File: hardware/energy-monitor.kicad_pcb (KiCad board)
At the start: 2 copper layers, 40 x 40 mm, 36 parts, among them P1 CON-SENSOR2, P3 BOOT, P4 DEBUG, U1 XMC110024, U2 TLV272IS, U3 DRILL, U4 DRILL, U5 DRILL, U6 DRILL, U7 phone-jack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

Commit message: fix sym lib table, change pcb texts
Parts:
- moved G*** 33.5 mm to (146.4, 73.9)
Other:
- board text added: "AC Current max 1V"
- board text added: "AC Voltage max 12VAC"
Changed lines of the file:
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@@
   (general
     (thickness 1.6)
-    (drawings 11)
+    (drawings 13)
     (tracks 228)
     (zones 0)
@@
   )
   (layers
-    (0 F.Cu signal)
-    (31 B.Cu signal)
+    (0 F.Cu signal hide)
+    (31 B.Cu signal hide)
     (32 B.Adhes user)
     (33 F.Adhes user)
@@
   )
   (setup
-    (last_trace_width 0.2)
+    (last_trace_width 0.25)
     (user_trace_width 0.2)
     (user_trace_width 0.3)
@@
   )
   (module kicad-libraries:Logo_31x31 (layer F.Cu)
-    (at 165.8 101.2)
+    (at 146.4 73.9)
     (fp_text reference G*** (at 0 0) (layer F.SilkS) hide
       (effects (font (size 1.524 1.524) (thickness 0.3)))
@@
       (xy -0.55372 -1.41224) (xy -0.55372 -1.67132)) (layer B.SilkS) (width 0.00254))
   )
-  (gr_text "Energy Monitor 1.0" (at 165.8 66.4) (layer F.SilkS)
+  (gr_text "AC Current\nmax 1V\n" (at 167.4 71.8) (layer F.SilkS)
     (effects (font (size 0.8 0.8) (thickness 0.15)))
   )
-  (gr_text tinkerforge.com (at 165.8 103.6) (layer F.SilkS)
+  (gr_text "AC Voltage max 12VAC" (at 172.3 88.6) (layer F.SilkS)
     (effects (font (size 0.8 0.8) (thickness 0.15)))
   )
+  (gr_text "Energy Monitor 1.0" (at 146.6 93) (layer F.SilkS)
+    (effects (font (size 0.8 0.8) (thickness 0.15)))
+  )
+  (gr_text tinkerforge.com (at 146.4 76.6) (layer F.SilkS)
+    (effects (font (size 0.8 0.8) (thickness 0.15)))
+  )

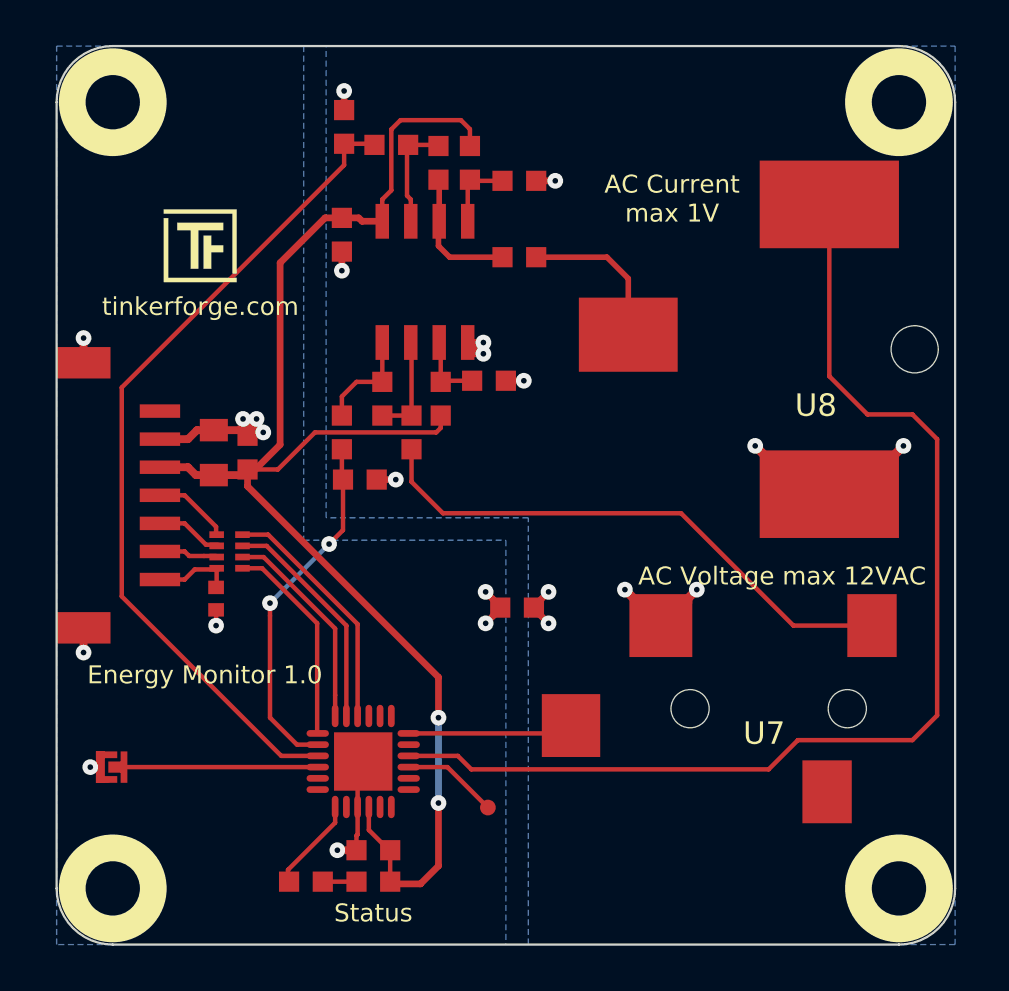
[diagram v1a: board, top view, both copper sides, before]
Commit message: changed text layout, added fiducialmarks, ready for prototype
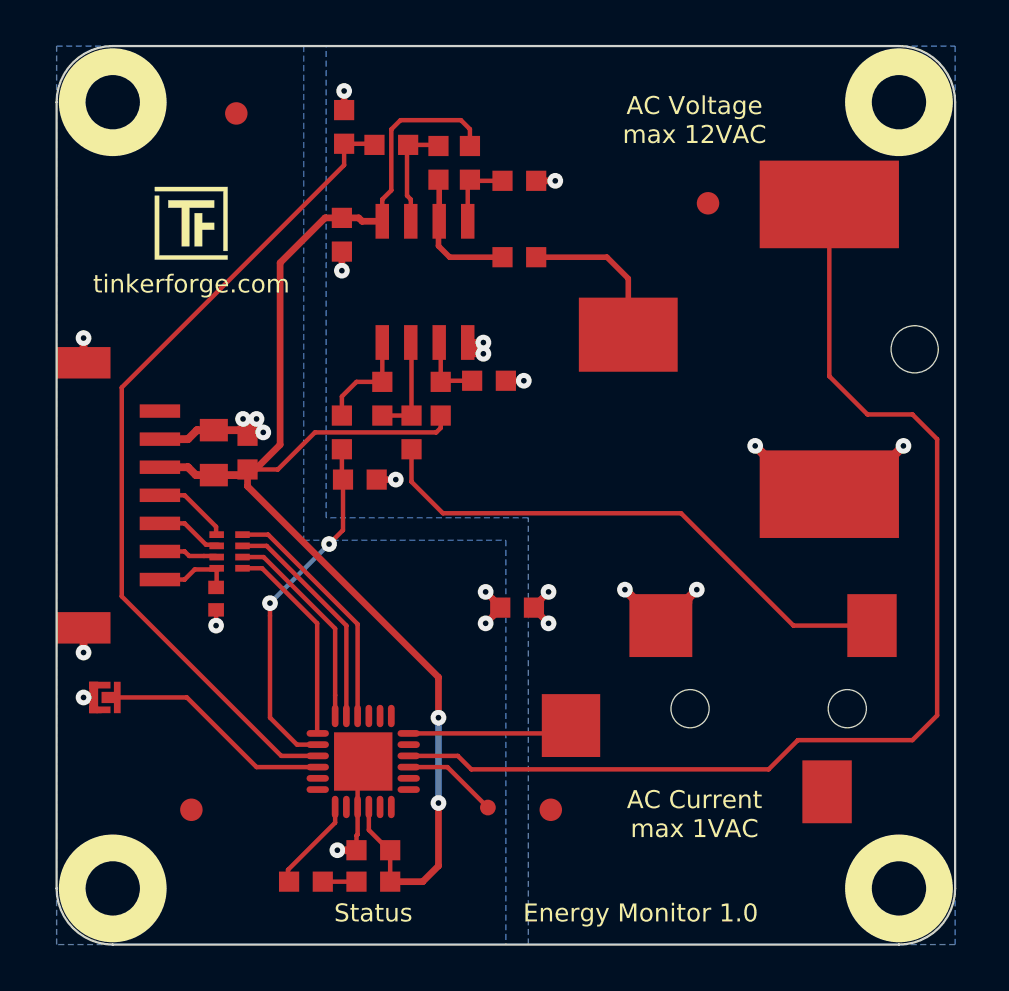
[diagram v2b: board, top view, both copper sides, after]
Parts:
- added Fiducial_Mark: VAL**, kicad-libraries:Fiducial_Mark, F.Cu at (148.0, 68.0)
- added Fiducial_Mark: VAL**, kicad-libraries:Fiducial_Mark, F.Cu at (146.0, 99.0)
- added Fiducial_Mark: VAL**, kicad-libraries:Fiducial_Mark, F.Cu at (169.0, 72.0)
- added Fiducial_Mark: VAL**, kicad-libraries:Fiducial_Mark, F.Cu at (162.0, 99.0)
- moved P3 3.11 mm to (142.2, 94.0)
- moved G*** 1.08 mm to (146.0, 72.9)
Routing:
- net Net-(P3-Pad2): track 8.93 -> 10.6 mm
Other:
- board text added: "AC Current max 1VAC"
- board text removed: "AC Current max 1V"

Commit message: changed resistor value for voltage measurement
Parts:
- R10, R9: value 3,9k -> 9,1k
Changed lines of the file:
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@@
   )
   (layers
-    (0 F.Cu signal)
+    (0 F.Cu signal hide)
     (31 B.Cu signal)
     (32 B.Adhes user)
-    (33 F.Adhes user)
+    (33 F.Adhes user hide)
     (34 B.Paste user)
-    (35 F.Paste user)
+    (35 F.Paste user hide)
     (36 B.SilkS user)
-    (37 F.SilkS user)
+    (37 F.SilkS user hide)
     (38 B.Mask user)
-    (39 F.Mask user)
+    (39 F.Mask user hide)
     (40 Dwgs.User user)
     (41 Cmts.User user)
@@
       (effects (font (size 0.2 0.2) (thickness 0.05)))
     )
-    (fp_text value 3,9k (at 0.05 -0.375 90) (layer F.Fab)
+    (fp_text value 9,1k (at 0.05 -0.375 90) (layer F.Fab)
       (effects (font (size 0.2 0.2) (thickness 0.05)))
     )
@@
       (effects (font (size 0.2 0.2) (thickness 0.05)))
     )
-    (fp_text value 3,9k (at 0.05 -0.375) (layer F.Fab)
-      (effects (font (size 0.2 0.2) (thickness 0.05)))
-    )
+    (fp_text value 9,1k (at 0.05 -0.375) (layer F.Fab)
+      (effects (font (size 0.2 0.2) (thickness 0.05)))
+    )

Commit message: changed resistor values
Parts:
- R3: value 22k -> 91k
- R4: value 3k -> 9,1k
- R5: value 15k -> 68k
- R6: value 12k -> 33k
- R9: value 9,1k -> 5,6k
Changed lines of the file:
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@@
       (effects (font (size 0.2 0.2) (thickness 0.05)))
     )
-    (fp_text value 22k (at 0.05 -0.375 270) (layer F.Fab)
+    (fp_text value 91k (at 0.05 -0.375 270) (layer F.Fab)
       (effects (font (size 0.2 0.2) (thickness 0.05)))
     )
@@
       (effects (font (size 0.2 0.2) (thickness 0.05)))
     )
-    (fp_text value 3k (at 0.05 -0.375) (layer F.Fab)
+    (fp_text value 9,1k (at 0.05 -0.375) (layer F.Fab)
       (effects (font (size 0.2 0.2) (thickness 0.05)))
     )
@@
       (effects (font (size 0.2 0.2) (thickness 0.05)))
     )
-    (fp_text value 15k (at 0.05 -0.375 270) (layer F.Fab)
+    (fp_text value 68k (at 0.05 -0.375 270) (layer F.Fab)
       (effects (font (size 0.2 0.2) (thickness 0.05)))
     )
@@
       (effects (font (size 0.2 0.2) (thickness 0.05)))
     )
-    (fp_text value 12k (at 0.05 -0.375 270) (layer F.Fab)
+    (fp_text value 33k (at 0.05 -0.375 270) (layer F.Fab)
       (effects (font (size 0.2 0.2) (thickness 0.05)))
     )
@@
       (effects (font (size 0.2 0.2) (thickness 0.05)))
     )
-    (fp_text value 9,1k (at 0.05 -0.375 90) (layer F.Fab)
+    (fp_text value 5,6k (at 0.05 -0.375 90) (layer F.Fab)
       (effects (font (size 0.2 0.2) (thickness 0.05)))
     )

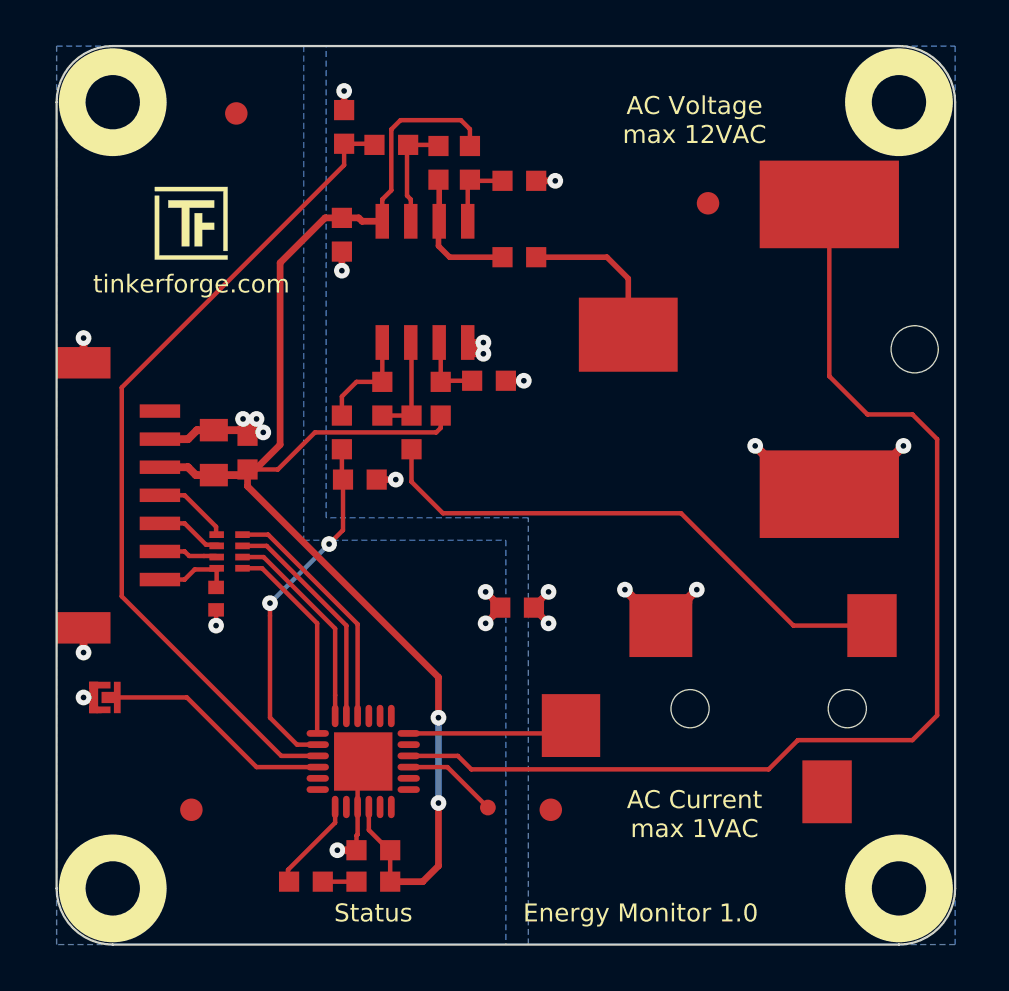
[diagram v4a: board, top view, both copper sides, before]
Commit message: changed resistor values, bigger footprint for dc-033, changed labeling
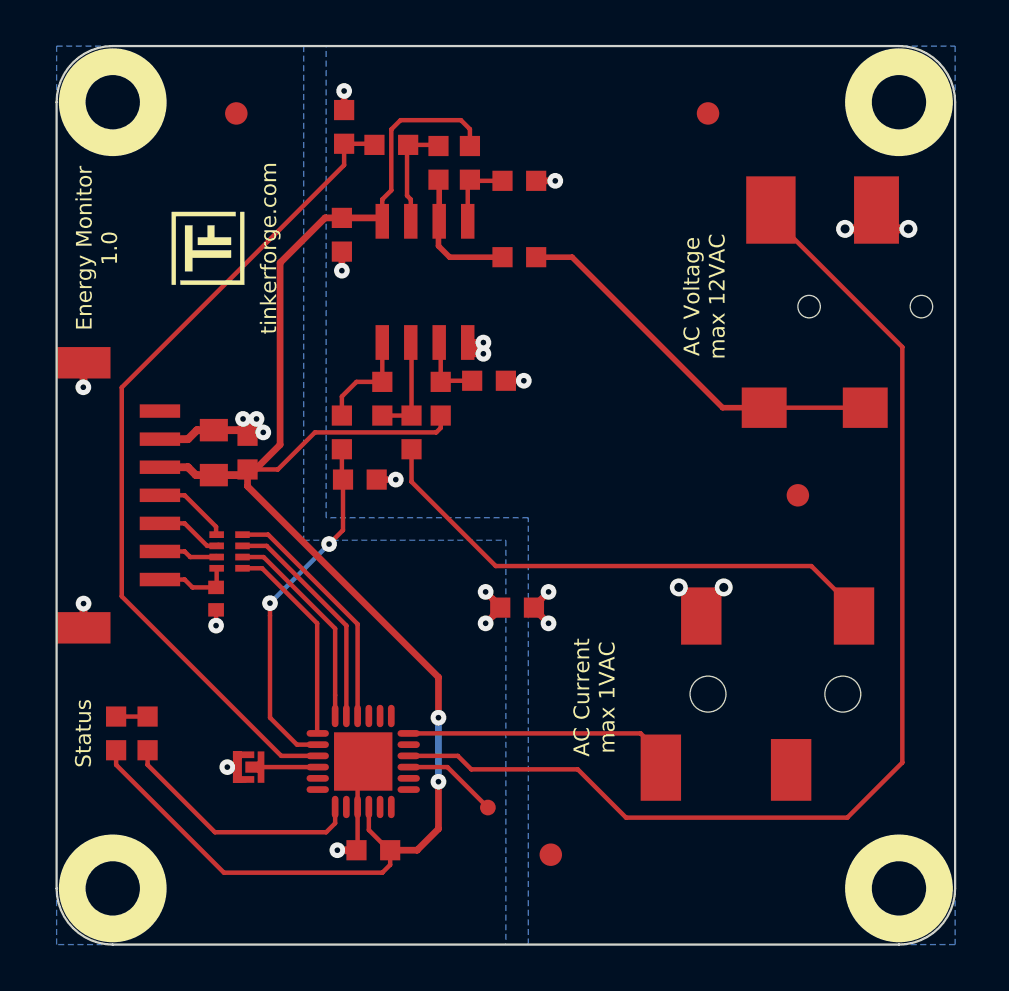
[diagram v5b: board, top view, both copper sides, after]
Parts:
- U7: footprint kicad-libraries:SJ-3524-SMT -> kicad-libraries:PJ-327C-3
- U8: footprint kicad-libraries:PJ-036AH-SMT -> kicad-libraries:DC-033
- moved Fiducial_Mark 30.4 mm to (173.0, 85.0)
- moved D3 13.2 mm to (142.7, 95.6), turned to 90 degrees
- moved G*** 9.91 mm to (160.0, 78.0), turned to 270 degrees
- moved R8 9.66 mm to (144.1, 95.6), turned to 90 degrees
- moved VAL 9.04 mm to (160.0, 91.4), turned to 270 degrees
- moved P3 7.11 mm to (148.6, 97.1)
- moved U8 6.51 mm to (180.0, 76.6)
- moved Fiducial_Mark 4.00 mm to (169.0, 68.0)
- moved U7 3.84 mm to (177.5, 93.8)
- moved Fiducial_Mark 2.00 mm to (162.0, 101.0)
- moved G*** 1.33 mm to (146.8, 74.0), turned to 90 degrees
- turned VAL to 270 degrees
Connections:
- P1 pad 1: (no net) -> +5V
- U1 pad 11: (no net) -> Net-(U1-Pad11)
- U1 pad 12: (no net) -> Net-(U1-Pad12)
- U1 pad 13: (no net) -> Net-(U1-Pad13)
- U1 pad 14: (no net) -> Net-(U1-Pad14)
- U1 pad 17: (no net) -> Net-(U1-Pad17)
- U1 pad 19: (no net) -> Net-(U1-Pad19)
- U1 pad 20: (no net) -> Net-(U1-Pad20)
- U1 pad 21: (no net) -> Net-(U1-Pad21)
- U1 pad 5: (no net) -> Net-(U1-Pad5)
- U1 pad 6: (no net) -> Net-(U1-Pad6)
- U1 pad 8: (no net) -> Net-(U1-Pad8)
- U7 pad 3: (no net) -> AGND
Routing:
- net 3V3: track 65.7 -> 78.3 mm
- net Net-(R11-Pad1): track 6.94 -> 18.1 mm
- net Net-(P3-Pad2): track 10.6 -> 3.22 mm
- net Net-(R8-Pad1): track 4.19 -> 11.1 mm
- net AGND: track 21.6 -> 16.5 mm
- net PlugA: track 7.55 -> 12.4 mm
- net PlugV: track 50.4 -> 51.2 mm
- net Net-(R5-Pad2): track 24.6 -> 23.9 mm
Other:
- net class Default: clearance 0.2 -> 0.149
- rule trace_clearance: 0.2 -> 0.149

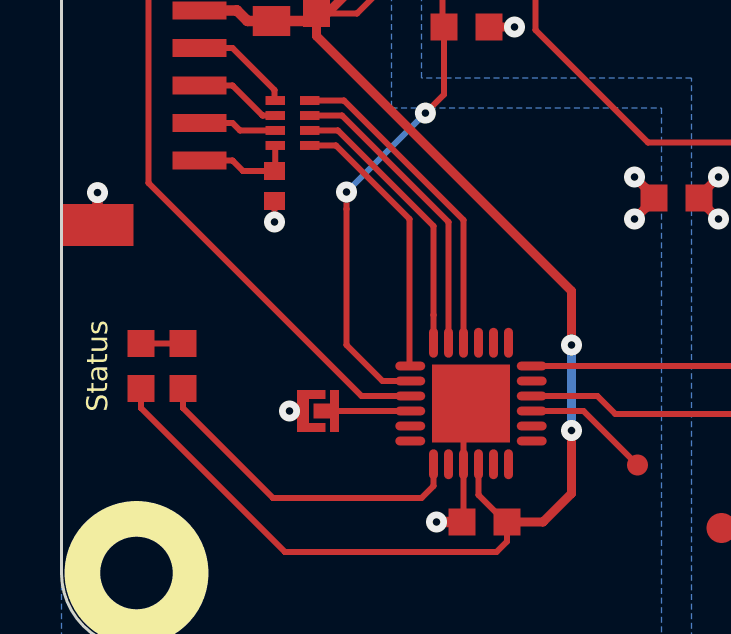
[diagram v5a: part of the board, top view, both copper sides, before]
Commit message: changed AnalogV pin from 2.2 to 2.7/2.8
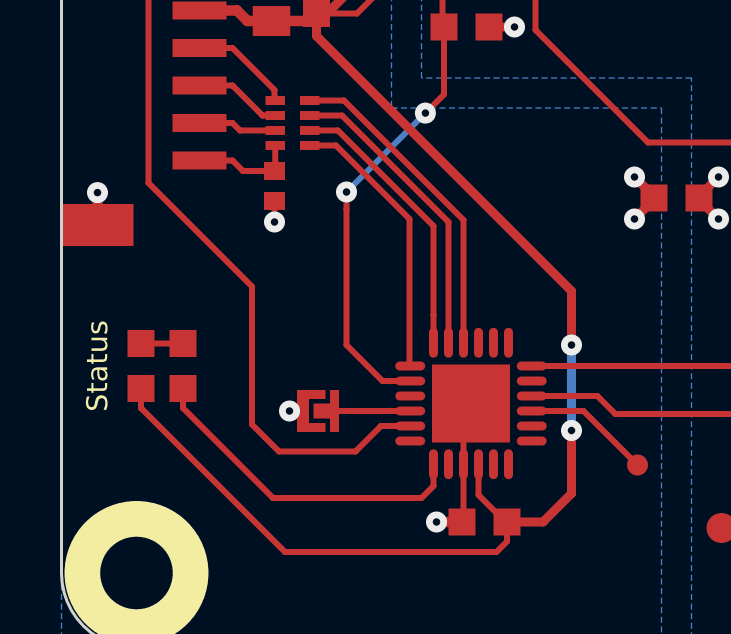
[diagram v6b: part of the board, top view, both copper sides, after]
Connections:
- U1 pad 3: AnalogV -> Net-(U1-Pad3)
- U1 pad 5: Net-(U1-Pad5) -> AnalogV
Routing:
- net AnalogV: track 37.4 -> 41.2 mm
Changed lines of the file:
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@@
     (thickness 1.6)
     (drawings 13)
-    (tracks 241)
+    (tracks 245)
     (zones 0)
     (modules 40)
@@
   )
   (setup
-    (last_trace_width 0.25)
+    (last_trace_width 0.2)
     (user_trace_width 0.2)
     (user_trace_width 0.3)
@@
   (net 27 PlugV)
   (net 28 +5V)
-  (net 29 "Net-(U1-Pad5)")
-  (net 30 "Net-(U1-Pad6)")
-  (net 31 "Net-(U1-Pad8)")
-  (net 32 "Net-(U1-Pad11)")
-  (net 33 "Net-(U1-Pad12)")
-  (net 34 "Net-(U1-Pad13)")
-  (net 35 "Net-(U1-Pad14)")
-  (net 36 "Net-(U1-Pad17)")
-  (net 37 "Net-(U1-Pad19)")
-  (net 38 "Net-(U1-Pad20)")
-  (net 39 "Net-(U1-Pad21)")
+  (net 29 "Net-(U1-Pad6)")
+  (net 30 "Net-(U1-Pad8)")
+  (net 31 "Net-(U1-Pad11)")
+  (net 32 "Net-(U1-Pad12)")
+  (net 33 "Net-(U1-Pad13)")
+  (net 34 "Net-(U1-Pad14)")
+  (net 35 "Net-(U1-Pad17)")
+  (net 36 "Net-(U1-Pad19)")
+  (net 37 "Net-(U1-Pad20)")
+  (net 38 "Net-(U1-Pad21)")
+  (net 39 "Net-(U1-Pad3)")
   (net_class Default "Dies ist die voreingestellte Netzklasse."
     (clearance 0.149)
@@
     (add_net "Net-(U1-Pad20)")
     (add_net "Net-(U1-Pad21)")
-    (add_net "Net-(U1-Pad5)")
+    (add_net "Net-(U1-Pad3)")
     (add_net "Net-(U1-Pad6)")
     (add_net "Net-(U1-Pad8)")
@@
       (net 4 AnalogA))
     (pad 3 smd oval (at -2.025 -0.25) (size 1 0.3) (layers F.Cu F.Paste F.Mask)
-      (net 5 AnalogV))
+      (net 39 "Net-(U1-Pad3)"))
     (pad 4 smd oval (at -2.025 0.25) (size 1 0.3) (layers F.Cu F.Paste F.Mask)
       (net 11 "Net-(P3-Pad2)"))
     (pad 5 smd oval (at -2.025 0.75) (size 1 0.3) (layers F.Cu F.Paste F.Mask)
-      (net 29 "Net-(U1-Pad5)"))
+      (net 5 AnalogV))
     (pad 6 smd oval (at -2.025 1.25) (size 1 0.3) (layers F.Cu F.Paste F.Mask)
-      (net 30 "Net-(U1-Pad6)"))
+      (net 29 "Net-(U1-Pad6)"))
     (pad 7 smd oval (at -1.25 2.025 90) (size 1 0.3) (layers F.Cu F.Paste F.Mask)
       (net 17 "Net-(R8-Pad1)"))
     (pad 8 smd oval (at -0.75 2.025 90) (size 1 0.3) (layers F.Cu F.Paste F.Mask)
-      (net 31 "Net-(U1-Pad8)"))
+      (net 30 "Net-(U1-Pad8)"))
     (pad 9 smd oval (at -0.25 2.025 90) (size 1 0.3) (layers F.Cu F.Paste F.Mask)
       (net 2 GND))
@@
       (net 1 3V3))
     (pad 11 smd oval (at 0.75 2.025 90) (size 1 0.3) (layers F.Cu F.Paste F.Mask)
-      (net 32 "Net-(U1-Pad11)"))
+      (net 31 "Net-(U1-Pad11)"))
     (pad 12 smd oval (at 1.25 2.025 90) (size 1 0.3) (layers F.Cu F.Paste F.Mask)
-      (net 33 "Net-(U1-Pad12)"))
+      (net 32 "Net-(U1-Pad12)"))
     (pad 13 smd oval (at 2.025 1.25) (size 1 0.3) (layers F.Cu F.Paste F.Mask)
-      (net 34 "Net-(U1-Pad13)"))
+      (net 33 "Net-(U1-Pad13)"))
     (pad 14 smd oval (at 2.025 0.75) (size 1 0.3) (layers F.Cu F.Paste F.Mask)
-      (net 35 "Net-(U1-Pad14)"))
+      (net 34 "Net-(U1-Pad14)"))
     (pad 15 smd oval (at 2.025 0.25) (size 1 0.3) (layers F.Cu F.Paste F.Mask)
       (net 12 "Net-(P4-Pad1)"))
@@
       (net 27 PlugV))
     (pad 17 smd oval (at 2.025 -0.75) (size 1 0.3) (layers F.Cu F.Paste F.Mask)
-      (net 36 "Net-(U1-Pad17)"))
+      (net 35 "Net-(U1-Pad17)"))
     (pad 18 smd oval (at 2.025 -1.25) (size 1 0.3) (layers F.Cu F.Paste F.Mask)
       (net 26 PlugA))
     (pad 19 smd oval (at 1.25 -2.025 90) (size 1 0.3) (layers F.Cu F.Paste F.Mask)
-      (net 37 "Net-(U1-Pad19)"))
+      (net 36 "Net-(U1-Pad19)"))
     (pad 20 smd oval (at 0.75 -2.025 90) (size 1 0.3) (layers F.Cu F.Paste F.Mask)
-      (net 38 "Net-(U1-Pad20)"))
+      (net 37 "Net-(U1-Pad20)"))
     (pad 21 smd oval (at 0.25 -2.025 90) (size 1 0.3) (layers F.Cu F.Paste F.Mask)
-      (net 39 "Net-(U1-Pad21)"))
+      (net 38 "Net-(U1-Pad21)"))
     (pad 22 smd oval (at -0.25 -2.025 90) (size 1 0.3) (layers F.Cu F.Paste F.Mask)
       (net 21 S-CS))
@@
   (segment (start 152.8 69.35) (end 154.15 69.35) (width 0.2) (layer F.Cu) (net 5))
   (segment (start 154.15 69.35) (end 154.2 69.4) (width 0.2) (layer F.Cu) (net 5))
-  (segment (start 150 96.6) (end 151.7 96.6) (width 0.2) (layer F.Cu) (net 5))
-  (segment (start 142.9 89.5) (end 150 96.6) (width 0.2) (layer F.Cu) (net 5))
+  (segment (start 149.8 98.45) (end 150.65 97.6) (width 0.2) (layer F.Cu) (net 5))
+  (segment (start 152.8 70.3) (end 142.9 80.2) (width 0.2) (layer F.Cu) (net 5))
+  (segment (start 150.65 97.6) (end 151.625 97.6) (width 0.2) (layer F.Cu) (net 5))
+  (segment (start 142.9 89.5) (end 146.35 92.95) (width 0.2) (layer F.Cu) (net 5))
+  (segment (start 152.8 69.35) (end 152.8 70.3) (width 0.2) (layer F.Cu) (net 5))
   (segment (start 142.9 80.2) (end 142.9 89.5) (width 0.2) (layer F.Cu) (net 5))
-  (segment (start 152.8 69.35) (end 152.8 70.3) (width 0.2) (layer F.Cu) (net 5))
-  (segment (start 152.8 70.3) (end 142.9 80.2) (width 0.2) (layer F.Cu) (net 5))
+  (segment (start 146.35 92.95) (end 146.35 97.55) (width 0.2) (layer F.Cu) (net 5))
+  (segment (start 147.25 98.45) (end 149.8 98.45) (width 0.2) (layer F.Cu) (net 5))
+  (segment (start 146.35 97.55) (end 147.25 98.45) (width 0.2) (layer F.Cu) (net 5))
   (segment (start 147.125 88.2493) (end 147.125 89.075) (width 0.2) (layer F.Cu) (net 6))
   (segment (start 147.125 89.075) (end 147.1 89.1) (width 0.2) (layer F.Cu) (net 6))
